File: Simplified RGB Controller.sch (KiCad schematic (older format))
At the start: 16 parts, among them IC1 SN74HCT245DBR, J1 RGB_3_pin, J2 RGB_3_pin, J3 RGB_3_pin, J4 RGB_3_pin, J5 RGB_3_pin, J6 RGB_3_pin, J7 RGB_3_pin, J8 RGB_3_pin, J9 AMP_Mate-N-Lok_Power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

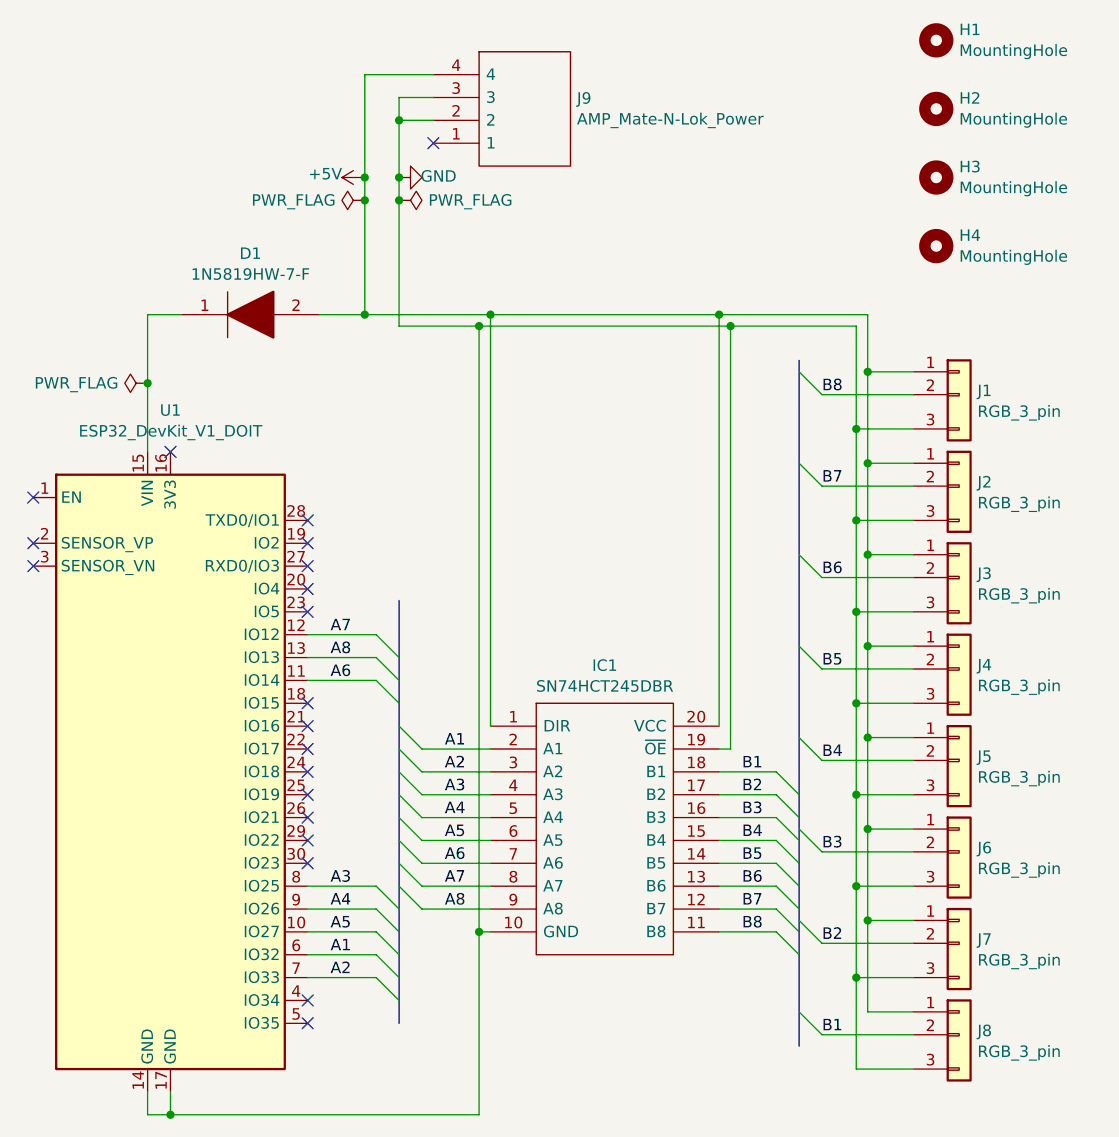
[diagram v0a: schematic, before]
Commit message: * Incoporate feedback * The ESP32 takes 12V on VIN
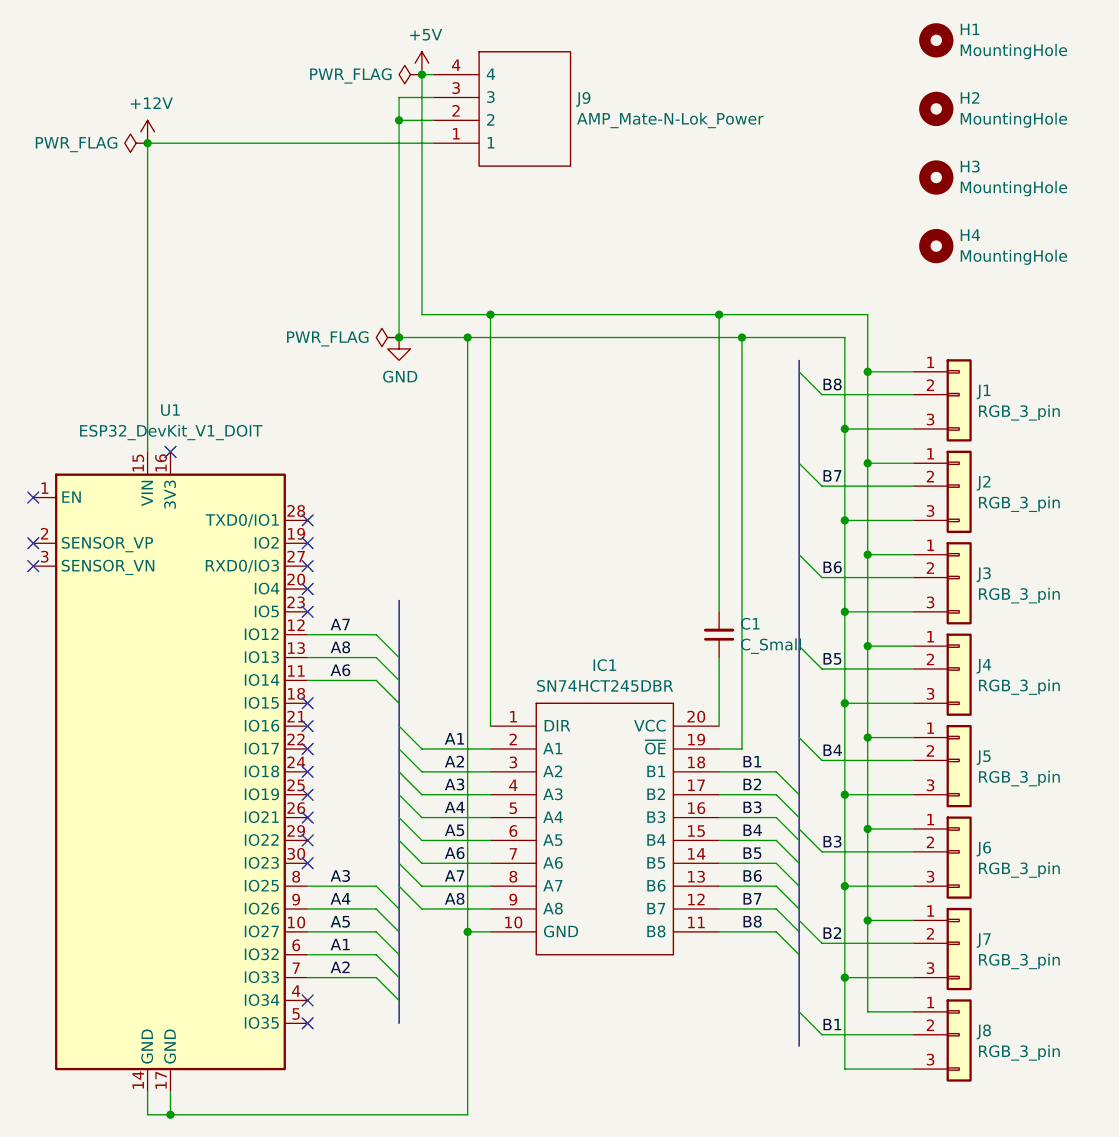
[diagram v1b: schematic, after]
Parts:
- removed D1: 1N5819HW-7-F, local:SOD3716X145N, symbol local:1N5819HW-7-F
- added C1: C_Small, Capacitor_SMD:C_0603_1608Metric_Pad1.08x0.95mm_HandSolder, symbol Device:C_Small
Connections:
- net +5V: now also C1.2; no longer IC1.20 (VCC)
- net +12V: now reaches U1.15 (VIN)
- net +12V: now also J9.1
- new net: C1.1, IC1.20 (VCC)
- no-connect marks 20 -> 19

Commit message: Update to match parts available at JCL.
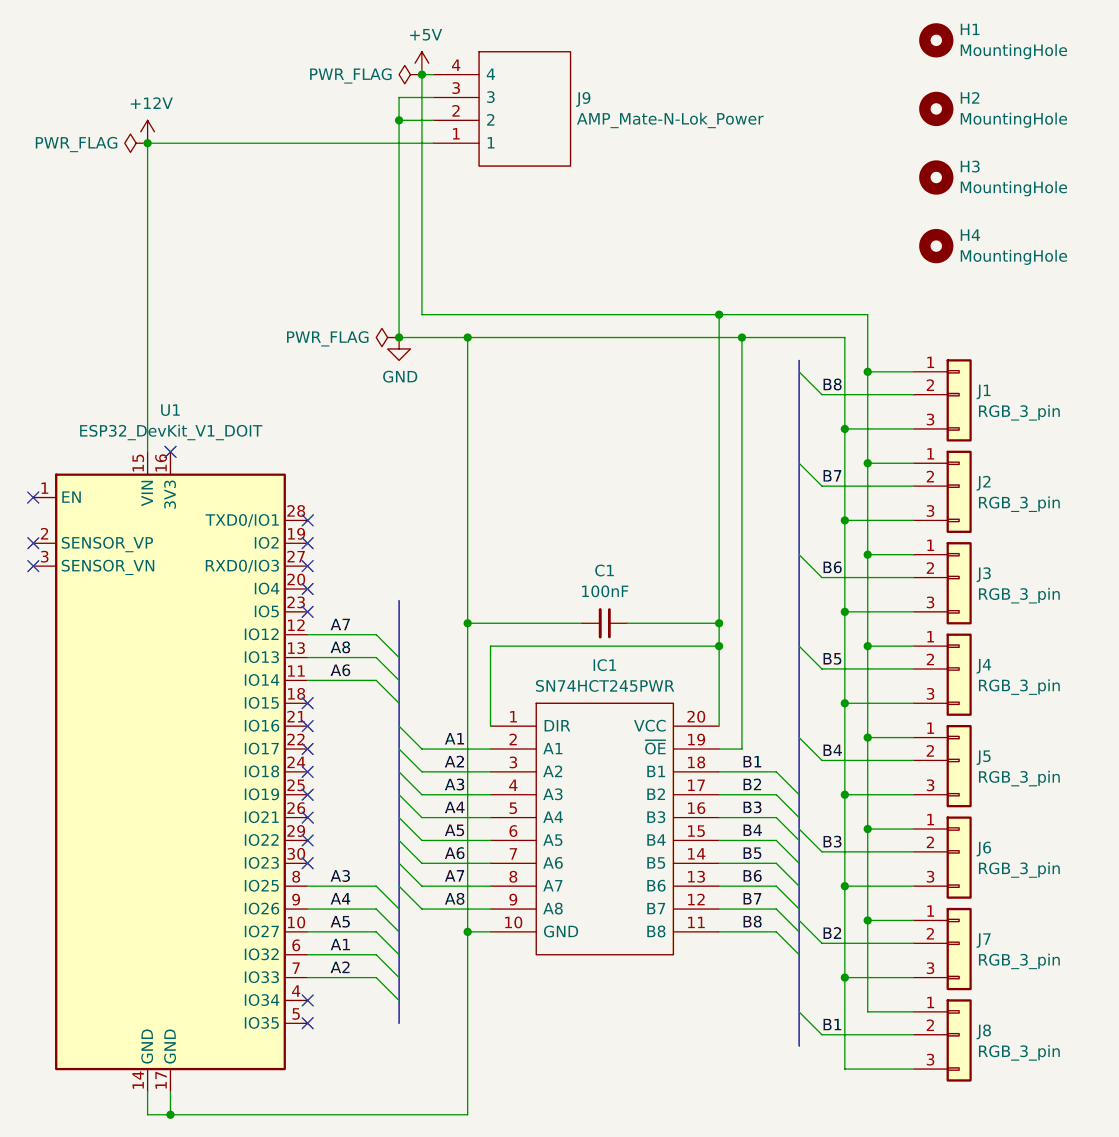
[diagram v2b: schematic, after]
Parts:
- removed IC1: SN74HCT245DBR, local:SN74HCT245DBR, symbol local:SN74HCT245DBR
- added IC1: SN74HCT245PWR, local:SN74HCT245PWR, symbol local:SN74HCT245PWR
- C1: value C_Small -> 100nF
- J9: footprint local:AMP_Mate_N_Lok -> local:TE_MATE-N-LOK_350211-1_1x04_P5.08mm_Vertical
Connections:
- net +5V: now also C1.1, IC1.1 (DIR), IC1.20 (VCC); no longer C1.2
- net A1: now also IC1.2 (A1)
- net A2: now also IC1.3 (A2)
- net A3: now also IC1.4 (A3)
- net A4: now also IC1.5 (A4)
- net A5: now also IC1.6 (A5)
- net A6: now also IC1.7 (A6)
- net A7: now also IC1.8 (A7)
- net A8: now also IC1.9 (A8)
- net B1: now also IC1.18 (B1)
- net B2: now also IC1.17 (B2)
- net B3: now also IC1.16 (B3)
- net B4: now also IC1.15 (B4)
- net B5: now also IC1.14 (B5)
- net B6: now also IC1.13 (B6)
- net B7: now also IC1.12 (B7)
- net B8: now also IC1.11 (B8)
- net GND: now also C1.2, IC1.10 (GND), IC1.19 (~OE)
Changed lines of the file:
@@
 $EndComp
-Wire Wire Line
-	3350 2600 3650 2600
 Wire Wire Line
 	3550 6100 2250 6100
@@
 Wire Wire Line
 	4650 4500 4750 4500
-Connection ~ 3650 2600
-Wire Wire Line
-	3650 2600 4650 2600
 Connection ~ 4650 2600
 Connection ~ 4750 2700
-Wire Wire Line
-	4650 4400 4650 4100
 Wire Wire Line
 	5300 4050 5500 4050
@@
 F 0 "J9" H 4028 1446 50  0000 L CNN
 F 1 "AMP_Mate-N-Lok_Power" H 4028 1355 50  0000 L CNN
-F 2 "local:AMP_Mate_N_Lok" H 4050 1650 50  0001 L CNN
+F 2 "local:TE_MATE-N-LOK_350211-1_1x04_P5.08mm_Vertical" H 4050 1650 50  0001 L CNN
 F 3 "http://uk.rs-online.com/web/p/products/0471430" H 4050 1550 50  0001 L CNN
 F 4 "Pin & Socket Connectors CONN PCM 4 POS TIN" H 4050 1450 50  0001 L CNN "Description"
@@
 Wire Wire Line
 	4650 4600 4900 4600
-$Comp
-L local:SN74HCT245DBR IC1
-U 1 1 60573DD7
-P 3650 4400
-F 0 "IC1" H 4150 4665 50  0000 C CNN
-F 1 "SN74HCT245DBR" H 4150 4574 50  0000 C CNN
-F 2 "local:SN74HCT245DBR" H 4500 4500 50  0001 L CNN
-F 3 "http://uk.rs-online.com/web/p/products/6628291P" H 4500 4400 50  0001 L CNN
-F 4 "Texas Instruments SN74HCT245DBR, Bus Transceiver, 8-Bit Non-Inverting CMOS, 5V, 20-Pin SSOP" H 4500 4300 50  0001 L CNN "Description"
-F 5 "2" H 4500 4200 50  0001 L CNN "Height"
-F 6 "6628291P" H 4500 4100 50  0001 L CNN "RS Part Number"
-F 7 "http://uk.rs-online.com/web/p/products/6628291P" H 4500 4000 50  0001 L CNN "RS Price/Stock"
-F 8 "Texas Instruments" H 4500 3900 50  0001 L CNN "Manufacturer_Name"
-F 9 "SN74HCT245DBR" H 4500 3800 50  0001 L CNN "Manufacturer_Part_Number"
-	1    3650 4400
-	1    0    0    -1
-$EndComp
 Text Label 3450 5200 0    50   ~ 0
 A8
@@
 	3250 2700 3550 2700
 Wire Wire Line
-	3550 2700 3550 5300
-Wire Wire Line
-	3650 4400 3650 2600
-$Comp
-L Device:C_Small C1
-U 1 1 605A5048
-P 4650 4000
-F 0 "C1" H 4558 3954 50  0000 R CNN
-F 1 "C_Small" H 4558 4045 50  0000 R CNN
-F 2 "Capacitor_SMD:C_0603_1608Metric_Pad1.08x0.95mm_HandSolder" H 4650 4000 50  0001 C CNN
-F 3 "~" H 4650 4000 50  0001 C CNN
-	1    4650 4000
-	-1   0    0    1
-$EndComp
-Wire Wire Line
-	4650 3900 4650 2600
+	3550 2700 3550 3950
 Wire Wire Line
 	4750 2700 4750 4500
@@
 	0    -1   -1   0
 $EndComp
+$Comp
+L Device:C_Small C1
+U 1 1 605A4D67
+P 4150 3950
+F 0 "C1" V 3921 3950 50  0000 C CNN
+F 1 "100nF" V 4012 3950 50  0000 C CNN
+F 2 "Capacitor_SMD:C_0603_1608Metric_Pad1.08x0.95mm_HandSolder" H 4150 3950 50  0001 C CNN
+F 3 "~" H 4150 3950 50  0001 C CNN
+	1    4150 3950
+	0    1    1    0
+$EndComp
+Wire Wire Line
+	4650 2600 4650 3950
+Wire Wire Line
+	4250 3950 4650 3950
+Connection ~ 4650 3950
+Wire Wire Line
+	4650 3950 4650 4050
+Connection ~ 3550 3950
+Wire Wire Line
+	3550 3950 3550 5300
+Wire Wire Line
+	3350 2600 4650 2600
+Wire Wire Line
+	3550 3950 4050 3950
+Wire Wire Line
+	3650 4400 3650 4050
+Wire Wire Line
+	3650 4050 4650 4050
+Connection ~ 4650 4050
+Wire Wire Line
+	4650 4050 4650 4400
 Wire Bus Line
 	5000 2800 5000 5800
 Wire Bus Line
 	3250 3850 3250 5700
+$Comp
+L local:SN74HCT245PWR IC1
+U 1 1 605EB202
+P 3650 4400
+F 0 "IC1" H 4150 4665 50  0000 C CNN
+F 1 "SN74HCT245PWR" H 4150 4574 50  0000 C CNN
+F 2 "local:SN74HCT245PWR" H 4500 4500 50  0001 L CNN
+F 3 "http://www.ti.com/general/docs/suppproductinfo.tsp?distId=10&gotoUrl=http%3A%2F%2Fwww.ti.com%2Flit%2Fgpn%2Fsn74hct245" H 4500 4400 50  0001 L CNN
+F 4 "Octal Bus Transceivers With 3-State Outputs" H 4500 4300 50  0001 L CNN "Description"
+F 5 "1.2" H 4500 4200 50  0001 L CNN "Height"
+F 6 "Texas Instruments" H 4500 4100 50  0001 L CNN "Manufacturer_Name"
+F 7 "SN74HCT245PWR" H 4500 4000 50  0001 L CNN "Manufacturer_Part_Number"
+F 8 "595-SN74HCT245PWR" H 4500 3900 50  0001 L CNN "Mouser Part Number"
+F 9 "https://www.mouser.co.uk/ProductDetail/Texas-Instruments/SN74HCT245PWR?qs=pt%2FIv5r0EPdWdXnOChoseA%3D%3D" H 4500 3800 50  0001 L CNN "Mouser Price/Stock"
+F 10 "SN74HCT245PWR" H 4500 3700 50  0001 L CNN "Arrow Part Number"
+F 11 "https://www.arrow.com/en/products/sn74hct245pwr/texas-instruments" H 4500 3600 50  0001 L CNN "Arrow Price/Stock"
+	1    3650 4400
+	1    0    0    -1
+$EndComp
 $EndSCHEMATC
